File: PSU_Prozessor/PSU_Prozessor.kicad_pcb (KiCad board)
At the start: 2 copper layers, 192.4 x 77 mm, 88 parts, among them IC1 6N138S, J1 ACJS-MHOP, J2 Conn_01x06, J3 FC68148S, J4 USB2066-05-RBHM-15-STB-00-01-A, J7 USB2066-05-RBHM-15-STB-00-01-A, Q1 BC847, Q2 2N7002, Q3 BC847, Q4 2N7002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

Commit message: Multiple enclosure versions
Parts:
- moved J4 1.20 mm to (235.0, 131.0)
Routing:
- net /USB5: track 215.3 -> 216.6 mm
- net /USB4: track 216.5 -> 217.8 mm
- net /USB3: track 218.0 -> 219.2 mm
- net /USB1: track 221.4 -> 222.7 mm
- net /USB2: track 219.6 -> 220.9 mm

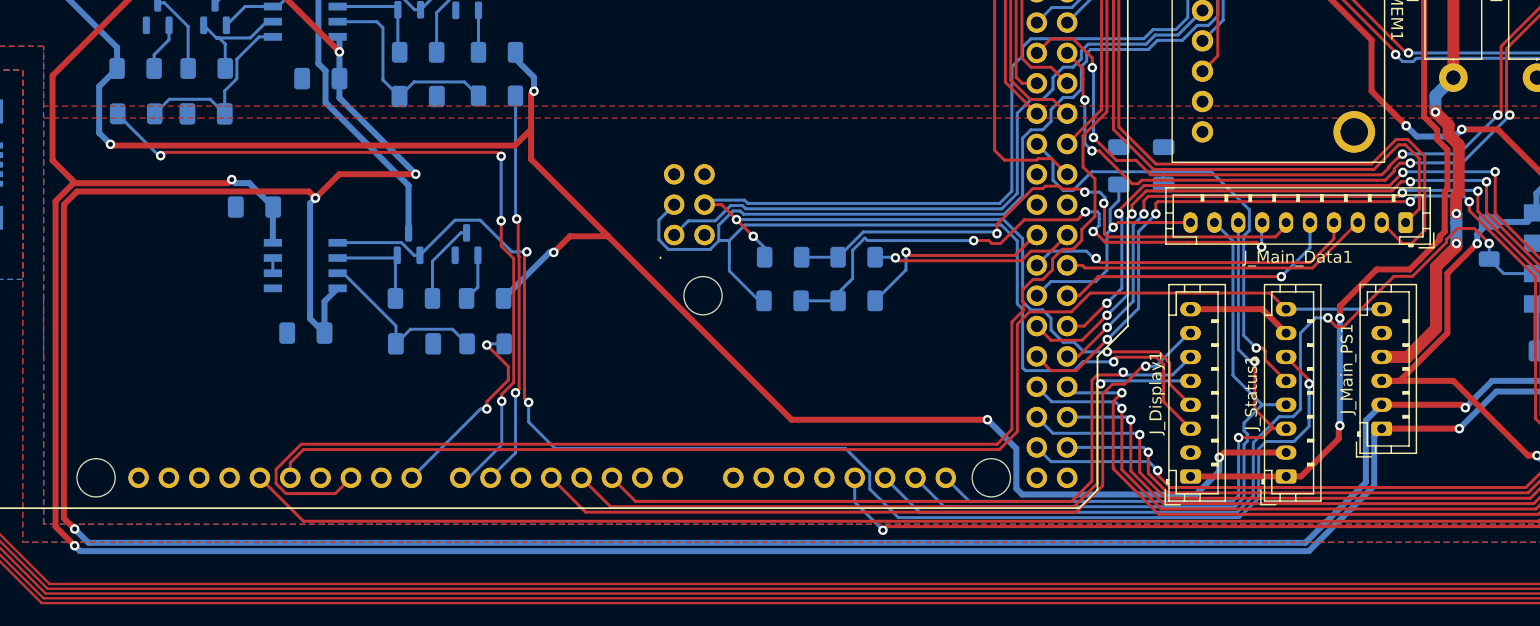
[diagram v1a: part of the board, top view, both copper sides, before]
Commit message: Added chip select for amps on main pcb
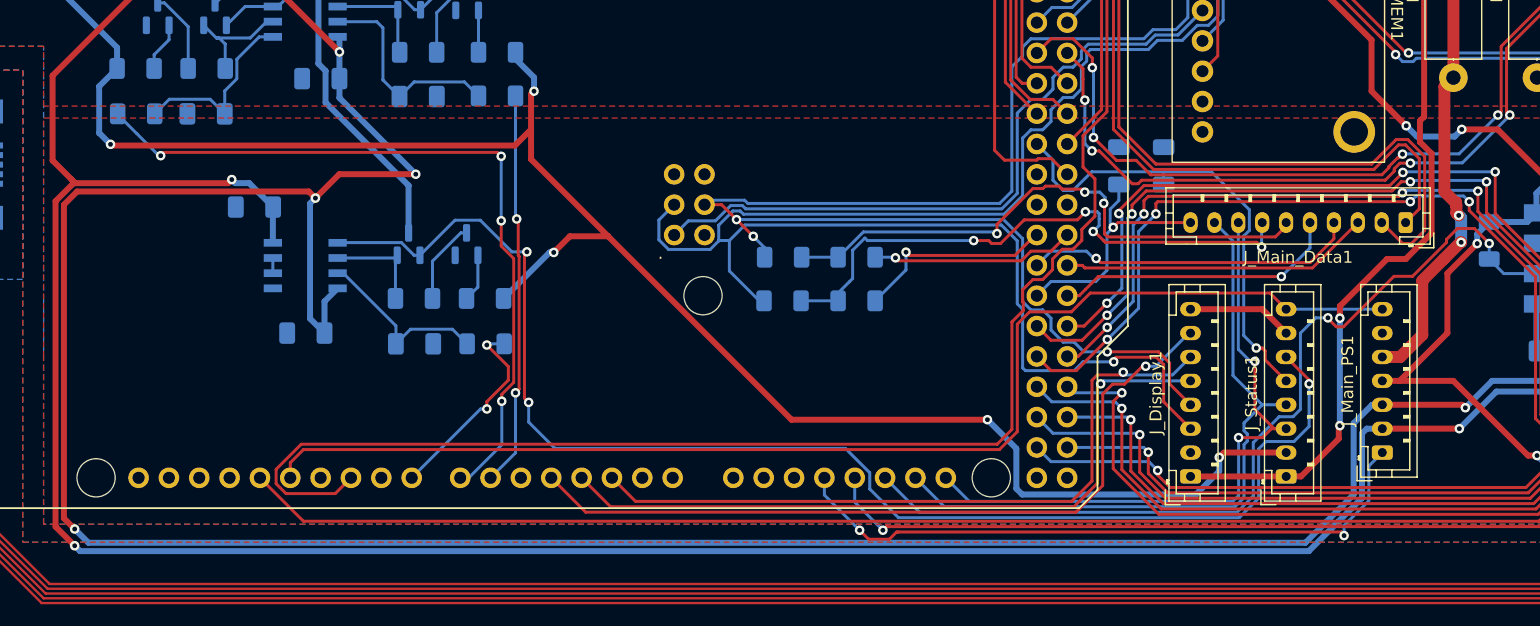
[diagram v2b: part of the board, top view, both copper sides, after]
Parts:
- J_Main_PS1: value Conn_01x06 -> Conn_01x07; footprint Connector_JST:JST_PH_B6B-PH-K_1x06_P2.00mm_Vertical -> Connector_JST:JST_PH_B7B-PH-K_1x07_P2.00mm_Vertical
- moved J_Main_PS1 2.00 mm to (171.1, 124.0)
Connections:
- J_Main_PS1 pad 1: /VDD15V0 -> /CS_Amp_N
- J_Main_PS1 pad 2: /VSS15V0 -> /VDD15V0
- J_Main_PS1 pad 3: /VDD3V3 -> /VSS15V0
- J_Main_PS1 pad 4: /VDD5V0 -> /VDD3V3
- J_Main_PS1 pad 5: GND -> /VDD5V0
- J_Main_PS1 pad 6: /I2C_Reset -> GND
- J_Swtich_Lower2 pad 8: /SER_Out_Lower -> unconnected-(J_Swtich_Lower2-Pad8)
- J_Swtich_Upper2 pad 8: /SER_Out_Upper -> unconnected-(J_Swtich_Upper2-Pad8)
- XA1 pad D17: unconnected-(XA1-PadD17) -> /CS_Amp_N
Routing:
- net /CS_Amp_N: track 0.00 -> 55.2 mm, vias 0 -> 2
- net /VDD3V3: track 393.1 -> 391.5 mm
- net /VDD9V0: track 270.7 -> 269.2 mm
- net /VDD5V0: track 199.5 -> 198.7 mm, vias 9 -> 8
- net /VDD15V0: track 257.2 -> 257.9 mm
